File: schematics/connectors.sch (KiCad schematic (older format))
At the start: 53 parts, among them J1 9V_BATTERY, J2 12V_DC_JACK, U1 LT3032-3.3, U2 STM32F103C8Tx, Y1 Crystal, Y2 Crystal

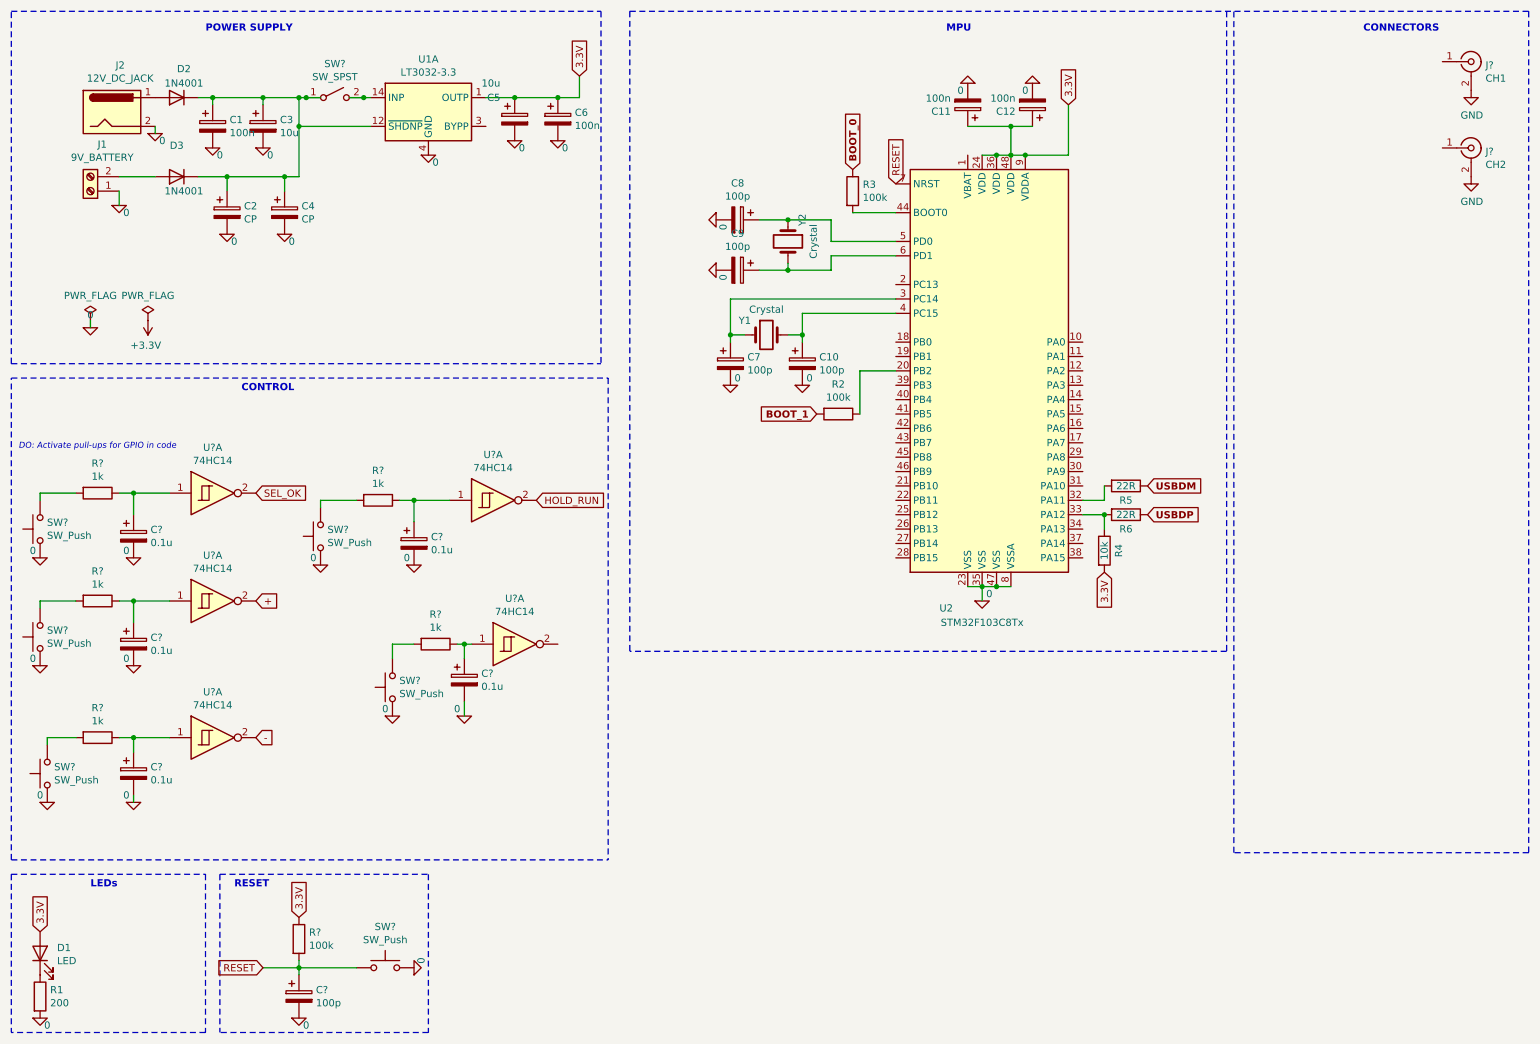
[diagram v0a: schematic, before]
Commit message: add 5V label for buffer
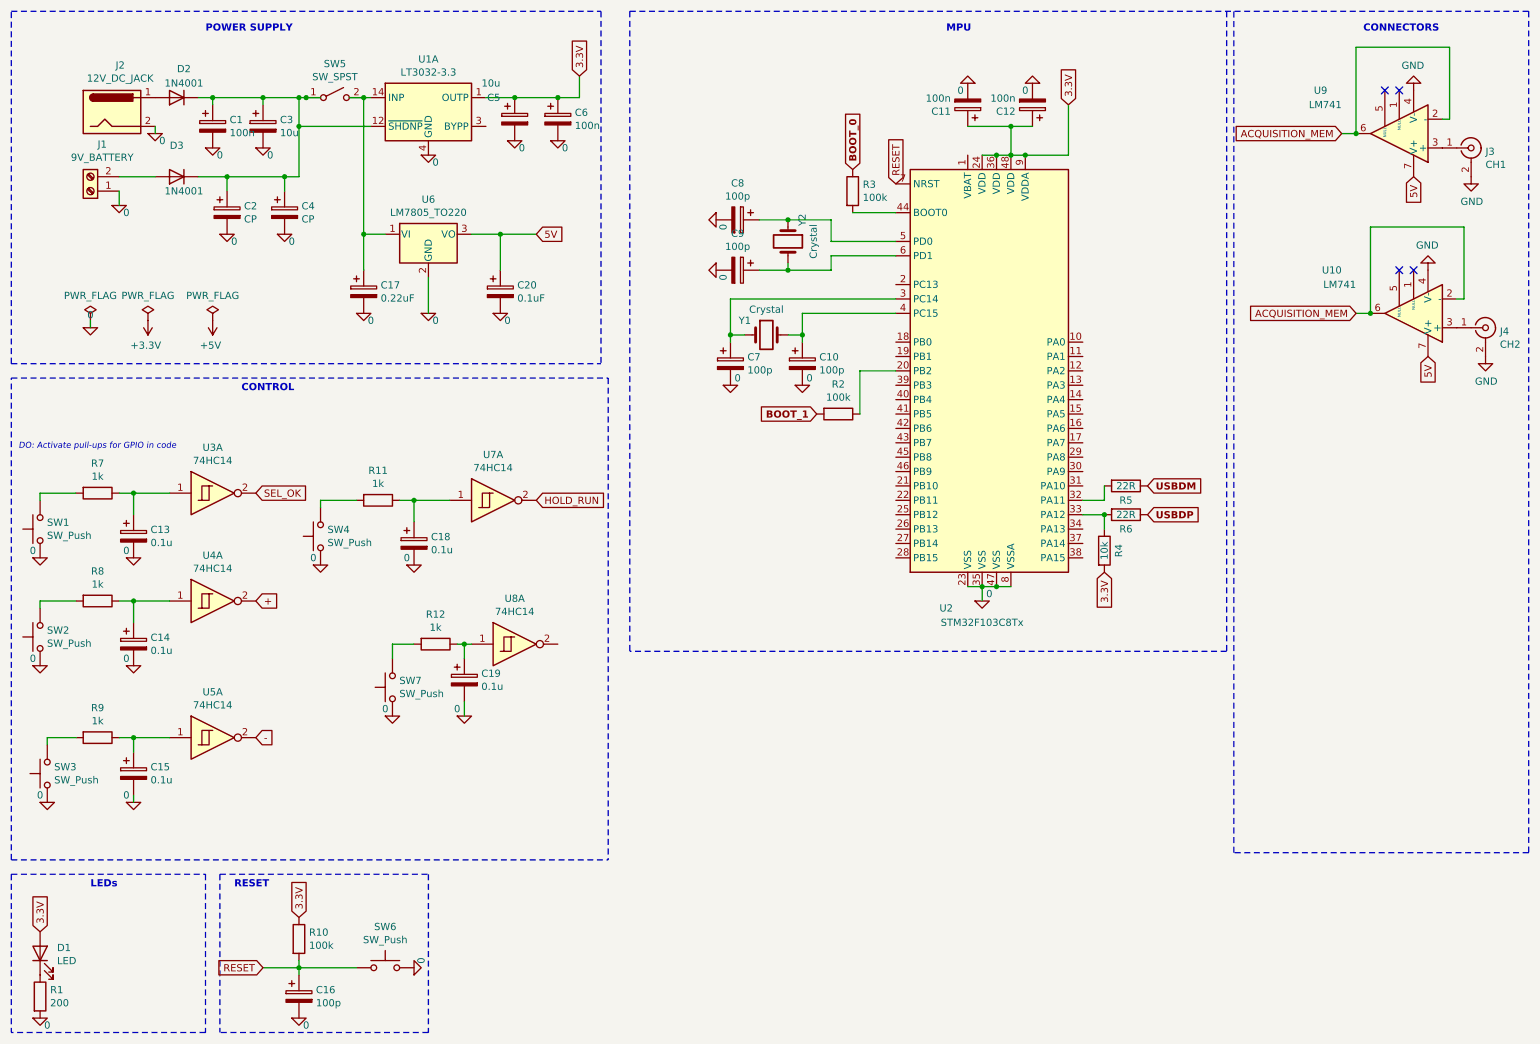
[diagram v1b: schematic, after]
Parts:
- added C17: 0.22uF, symbol Device:CP
- added C20: 0.1uF, symbol Device:CP
- added U10, U9: LM741, symbol Amplifier_Operational:LM741
- added U6: LM7805_TO220, Package_TO_SOT_THT:TO-220-3_Vertical, symbol Regulator_Linear:LM7805_TO220
- gave numbers to parts that had none: 26
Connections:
- net 0: now also C17.2, C20.2, U6.2 (GND)
- net GND: now also U10.4 (V-), U9.4 (V-)
- net at SW5.2 (B), U1.14 (INP): now also C17.1, U6.1 (VI)
- net at J3.1 (In): now also U9.3 (+)
- net at J4.1 (In): now also U10.3 (+)
- new net 5V: C20.1, U10.7 (V+), U6.3 (VO), U9.7 (V+)
- new net ACQUISITION_MEM: U10.2 (-), U10.6, U9.2 (-), U9.6
- no-connect marks 0 -> 4
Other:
- moved on the sheet: J3, J4
